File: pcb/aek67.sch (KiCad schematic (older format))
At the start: 20 parts

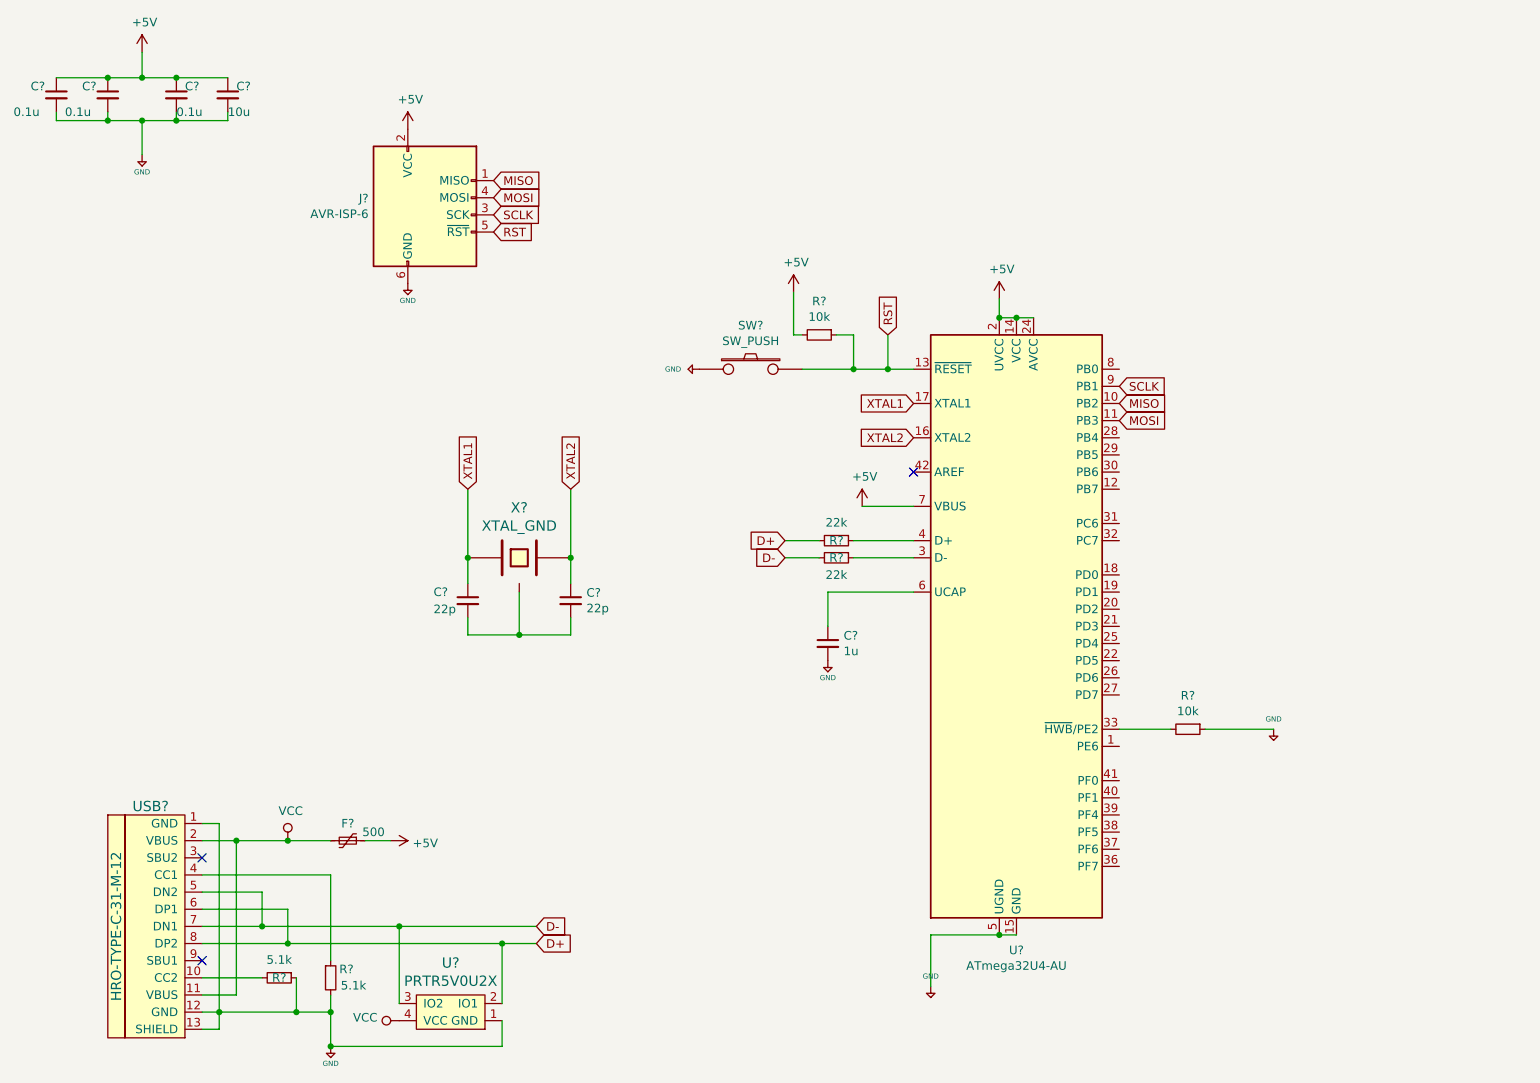
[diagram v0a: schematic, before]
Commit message: Added matrix and footprints
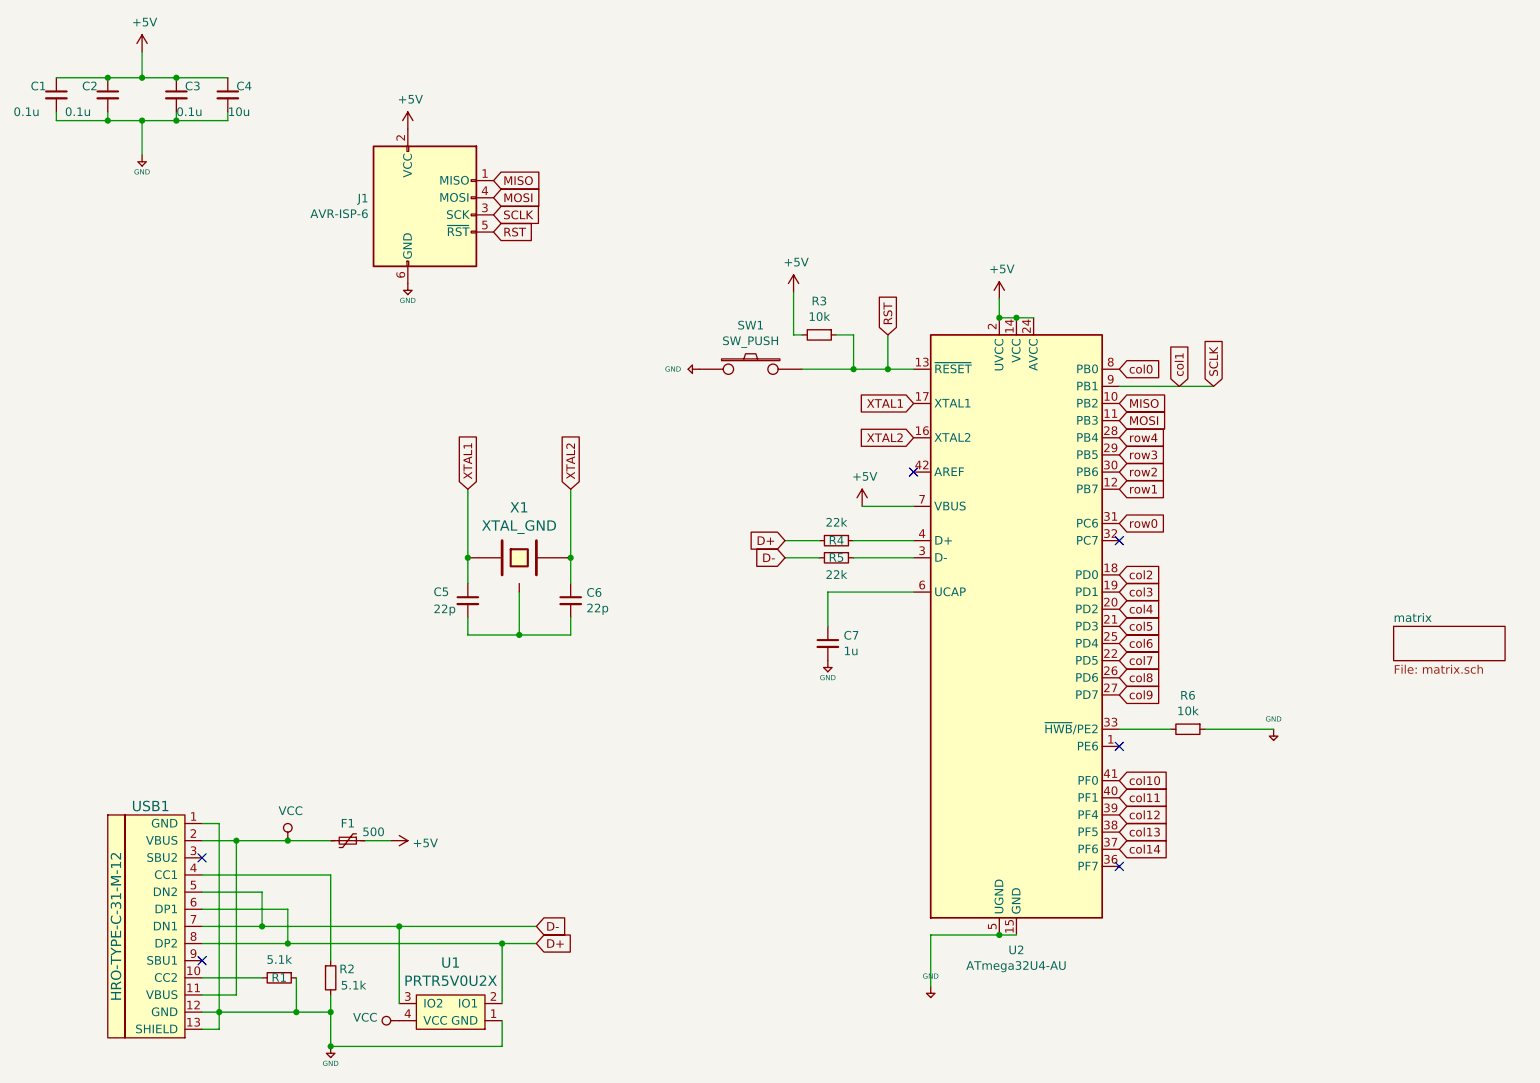
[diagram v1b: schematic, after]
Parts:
- C1, C2, C3, C4, C5, C6, C7: renamed from C?; footprint (none) -> Diode_SMD:D_SOD-123
- F1: renamed from F?; footprint (none) -> Fuse:Fuse_1206_3216Metric_Pad1.42x1.75mm_HandSolder
- J1: renamed from J?; footprint (none) -> random-keyboard-parts:Reset_Pretty-Mask
- R1, R2, R3, R4, R5, R6: renamed from R?; footprint (none) -> Resistor_SMD:R_0805_2012Metric_Pad1.15x1.40mm_HandSolder
- SW1: renamed from SW?; footprint (none) -> random-keyboard-parts:SKQG-1155865
- U1: renamed from U?; footprint (none) -> local:SOT143B
- USB1: renamed from USB?; footprint (none) -> Type-C:HRO-TYPE-C-31-M-12-HandSoldering
- X1: renamed from X?; footprint (none) -> Crystal:Crystal_SMD_3225-4Pin_3.2x2.5mm_HandSoldering
- gave numbers to parts that had none: 1
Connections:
- net row1: now reaches U2.12 (PB7)
- net col2: now reaches U2.18 (PD0)
- net col3: now reaches U2.19 (PD1)
- net col4: now reaches U2.20 (PD2)
- net col5: now reaches U2.21 (PD3)
- net col7: now reaches U2.22 (PD5)
- net col6: now reaches U2.25 (PD4)
- net col8: now reaches U2.26 (PD6)
- net col9: now reaches U2.27 (PD7)
- net row4: now reaches U2.28 (PB4)
- net row3: now reaches U2.29 (PB5)
- net row2: now reaches U2.30 (PB6)
- net row0: now reaches U2.31 (PC6)
- net col14: now reaches U2.37 (PF6)
- net col13: now reaches U2.38 (PF5)
- net col12: now reaches U2.39 (PF4)
- net col11: now reaches U2.40 (PF1)
- net col10: now reaches U2.41 (PF0)
- net col0: now reaches U2.8 (PB0)
- no-connect marks 3 -> 6
